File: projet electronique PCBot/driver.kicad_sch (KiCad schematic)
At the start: 1 part, among them U4 DRV8833PWP

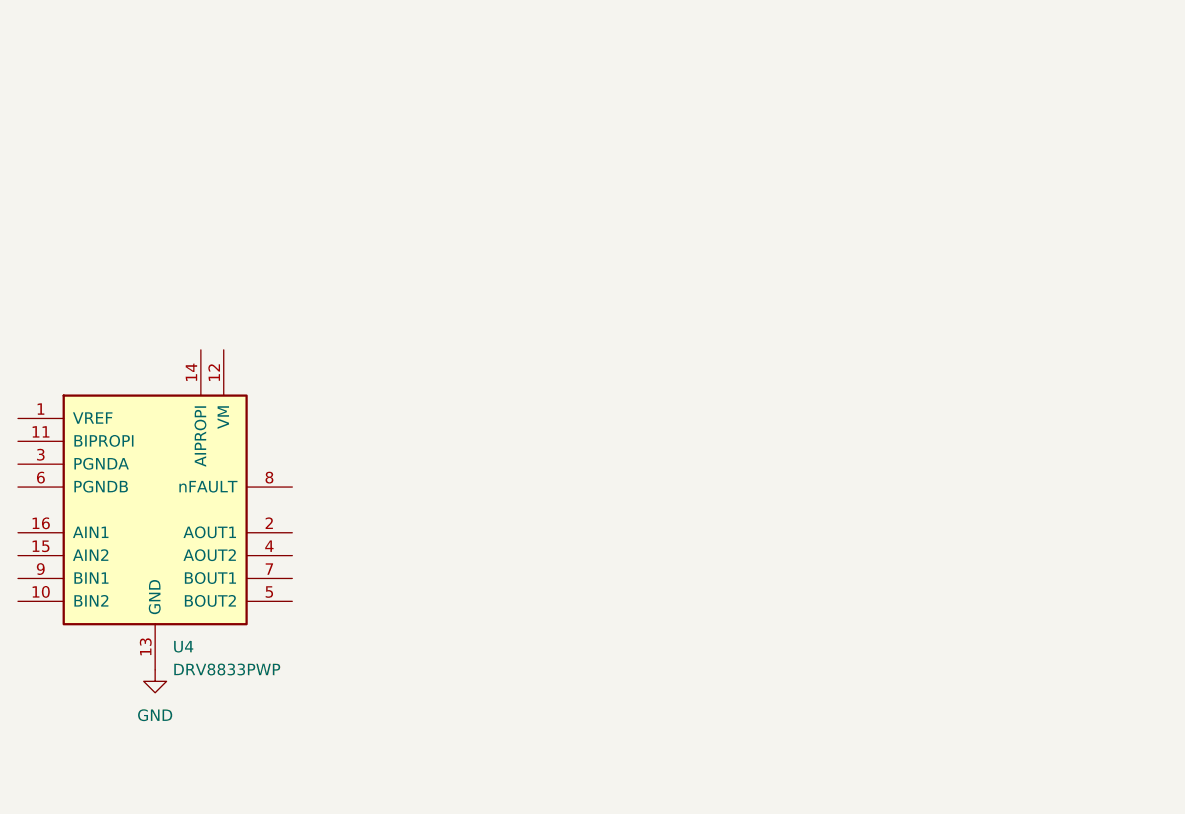
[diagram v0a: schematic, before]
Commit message: modification de la feuille driver
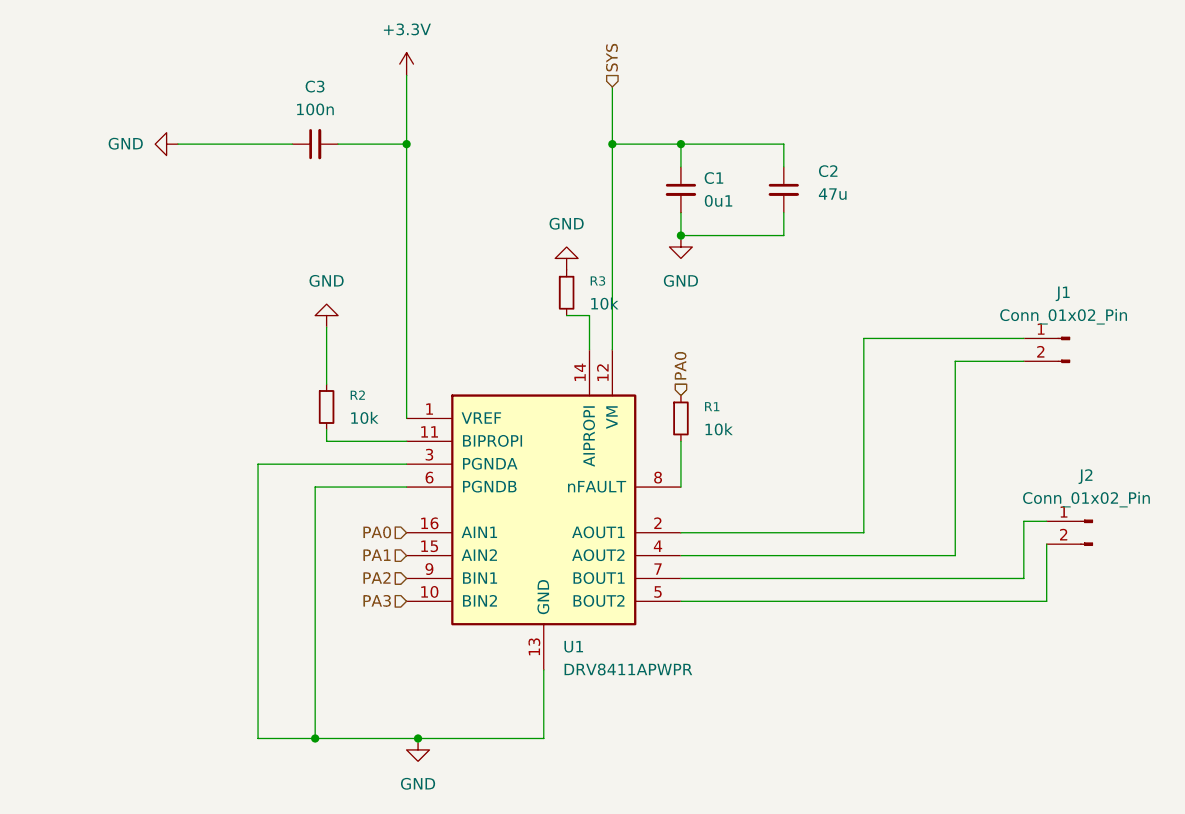
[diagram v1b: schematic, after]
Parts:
- removed U4: DRV8833PWP, Package_SO:HTSSOP-16-1EP_4.4x5mm_P0.65mm_EP3.4x5mm_Mask2.46x2.31mm_ThermalVias, symbol pcbot_lib:DRV8411APWPR
- added C1: 0u1, symbol Device:C_Small
- added C2: 47u, symbol Device:C_Small
- added C3: 100n, symbol Device:C_Small
- added J1, J2: Conn_01x02_Pin, symbol Connector:Conn_01x02_Pin
- added R1, R2, R3: 10k, symbol Device:R_Small
- added U1: DRV8411APWPR, Package_SO:HTSSOP-16-1EP_4.4x5mm_P0.65mm_EP3.4x5mm_Mask2.46x2.31mm_ThermalVias, symbol pcbot_lib:DRV8411APWPR
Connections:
- net GND: now also C1.2, C2.2, C3.1, R2.1, R3.1, U1.13 (GND), U1.17 (GND(PPAD)), U1.3 (PGNDA), U1.6 (PGNDB)
- new net: J2.1 (Pin_1), U1.7 (BOUT1)
- new net: J2.2 (Pin_2), U1.5 (BOUT2)
- new net: J1.1 (Pin_1), U1.2 (AOUT1)
- new net: J1.2 (Pin_2), U1.4 (AOUT2)
- new net: R2.2, U1.11 (BIPROPI)
- new net: R3.2, U1.14 (AIPROPI)
- new net: R1.2, U1.8 (nFAULT)
- new net +3.3V: C3.2, U1.1 (VREF)
- new net PA0: R1.1, U1.16 (AIN1)
- new net PA1: U1.15 (AIN2)
- new net PA2: U1.9 (BIN1)
- new net PA3: U1.10 (BIN2)
- new net SYS: C1.1, C2.1, U1.12 (VM)
